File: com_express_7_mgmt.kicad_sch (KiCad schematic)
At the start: 64 parts, among them J1 Plug_Bus_CE7_EPT_401-51501-51, Q1 BSS138-7-F, Q2 BSS138-7-F, SW1 SW_1-1825027-1_THT, SW2 SW_1-1825027-1_THT, SW3 SW_DS04-254-1-01BK-SMT, U30 MAX16150A_SOT, U31 74AUP2G132, U32 TPS3840PL30DBVR, U33 74AUP2G132, U34 W25Q32FV_SOIC-8, U35 M24C64-F_DFN8

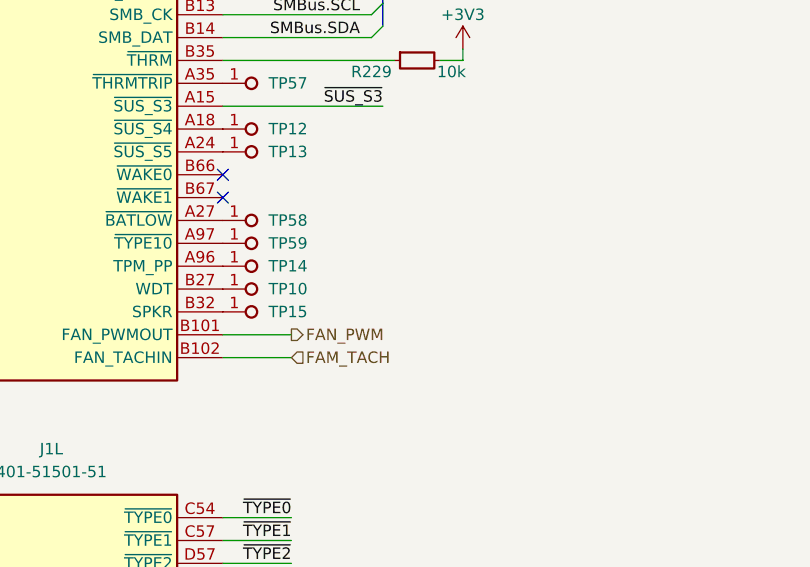
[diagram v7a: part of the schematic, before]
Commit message: [#57905] Add ADT7476AARQZ temperature/voltage/fan system monitor, LEDs
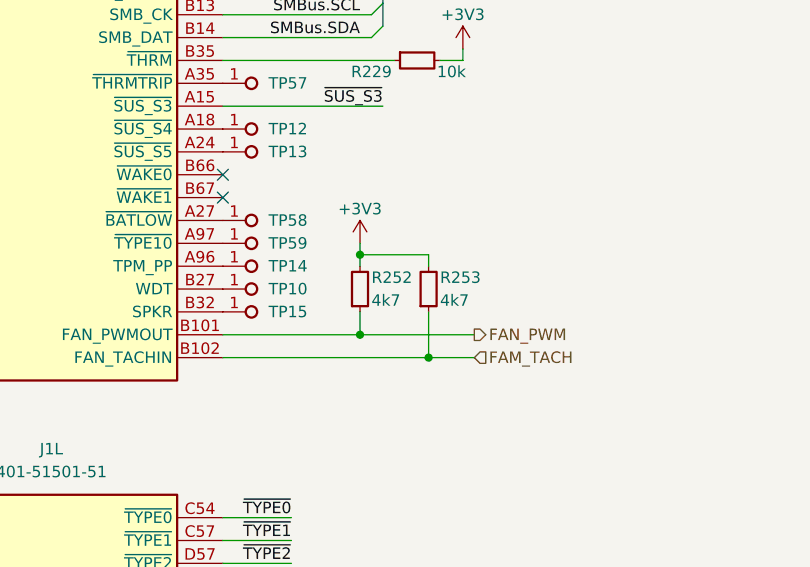
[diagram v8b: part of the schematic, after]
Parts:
- added R252, R253: R_4k7_0402, antmicro-footprints:R_0402_1005Metric, symbol antmicroResistors0402:R_4k7_0402
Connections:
- net +3V3: now also R252.2, R253.2
- net FAM_TACH: now also R253.1
- net FAN_PWM: now also R252.1
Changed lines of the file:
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@@
   (junction (at 217.17 78.74) (diameter 0) (color 0 0 0 0)
   )
+  (junction (at 91.44 184.15) (diameter 0) (color 0 0 0 0)
+  )
   (junction (at 356.87 193.04) (diameter 0) (color 0 0 0 0)
   )
@@
   (junction (at 336.55 41.91) (diameter 0) (color 0 0 0 0)
   )
+  (junction (at 91.44 193.04) (diameter 0) (color 0 0 0 0)
+  )
   (junction (at 228.6 218.44) (diameter 0) (color 0 0 0 0)
   )
@@
   )
   (junction (at 250.19 223.52) (diameter 0) (color 0 0 0 0)
+  )
+  (junction (at 99.06 195.58) (diameter 0) (color 0 0 0 0)
   )
   (junction (at 299.72 59.69) (diameter 0) (color 0 0 0 0)
@@
     (stroke (width 0) (type default))
   )
+  (wire (pts (xy 91.44 184.15) (xy 91.44 185.42))
+    (stroke (width 0) (type default))
+  )
   (wire (pts (xy 76.2 50.8) (xy 78.74 50.8))
     (stroke (width 0) (type default))
@@
     (stroke (width 0) (type default))
   )
+  (wire (pts (xy 91.44 182.88) (xy 91.44 184.15))
+    (stroke (width 0) (type default))
+  )
   (wire (pts (xy 311.15 190.5) (xy 323.85 190.5))
     (stroke (width 0) (type default))
@@
   )
   (wire (pts (xy 344.17 68.58) (xy 344.17 67.31))
+    (stroke (width 0) (type default))
+  )
+  (wire (pts (xy 99.06 184.15) (xy 99.06 185.42))
     (stroke (width 0) (type default))
   )
@@
     (stroke (width 0) (type default))
   )
+  (wire (pts (xy 91.44 184.15) (xy 99.06 184.15))
+    (stroke (width 0) (type default))
+  )
   (wire (pts (xy 280.67 137.16) (xy 283.21 137.16))
     (stroke (width 0) (type default))
@@
     (stroke (width 0) (type default))
   )
+  (wire (pts (xy 99.06 195.58) (xy 104.14 195.58))
+    (stroke (width 0) (type default))
+  )
   (bus (pts (xy 210.82 209.55) (xy 201.93 209.55))
     (stroke (width 0) (type default))
@@
     (stroke (width 0) (type default))
   )
+  (wire (pts (xy 91.44 190.5) (xy 91.44 193.04))
+    (stroke (width 0) (type default))
+  )
   (bus (pts (xy 316.23 207.01) (xy 316.23 204.47))
     (stroke (width 0) (type default))
@@
     (stroke (width 0) (type default))
   )
+  (wire (pts (xy 91.44 193.04) (xy 76.2 193.04))
+    (stroke (width 0) (type default))
+  )
   (wire (pts (xy 76.2 248.92) (xy 92.71 248.92))
     (stroke (width 0) (type default))
@@
     (stroke (width 0) (type default))
   )
-  (wire (pts (xy 83.82 193.04) (xy 76.2 193.04))
+  (wire (pts (xy 104.14 193.04) (xy 91.44 193.04))
     (stroke (width 0) (type default))
   )
@@
     (stroke (width 0) (type default))
   )
+  (wire (pts (xy 99.06 190.5) (xy 99.06 195.58))
+    (stroke (width 0) (type default))
+  )
   (wire (pts (xy 354.965 231.14) (xy 361.315 231.14))
     (stroke (width 0) (type default))
@@
     (stroke (width 0) (type default))
   )
-  (wire (pts (xy 76.2 195.58) (xy 83.82 195.58))
+  (wire (pts (xy 76.2 195.58) (xy 99.06 195.58))
     (stroke (width 0) (type default))
   )
@@
     (effects (font (size 1.27 1.27)) (justify right bottom))
   )
-  (hierarchical_label "FAM_TACH" (shape input) (at 83.82 195.58 0) (fields_autoplaced)
+  (hierarchical_label "FAM_TACH" (shape input) (at 104.14 195.58 0) (fields_autoplaced)
     (effects (font (size 1.27 1.27)) (justify left))
   )
@@
     (effects (font (size 1.27 1.27)) (justify left))
   )
-  (hierarchical_label "FAN_PWM" (shape output) (at 83.82 193.04 0) (fields_autoplaced)
+  (hierarchical_label "FAN_PWM" (shape output) (at 104.14 193.04 0) (fields_autoplaced)
     (effects (font (size 1.27 1.27)) (justify left))
   )
@@
     )
   )
+  (symbol (lib_id "antmicroResistors0402:R_4k7_0402") (at 91.44 190.5 90) (unit 1)
+    (in_bom yes) (on_board yes) (dnp no)
+    (property "Reference" "R252" (at 92.71 186.69 90)
+      (effects (font (size 1.27 1.27) (thickness 0.15)) (justify right))
+    )
+    (property "Value" "R_4k7_0402" (at 104.14 170.18 0)
+      (effects (font (size 1.27 1.27) (thickness 0.15)) (justify left bottom) hide)
+    )
+    (property "Footprint" "antmicro-footprints:R_0402_1005Metric" (at 106.68 170.18 0)
+      (effects (font (size 1.27 1.27) (thickness 0.15)) (justify left bottom) hide)
+    )
+    (property "Datasheet" "https://www.bourns.com/docs/product-datasheets/cr.pdf" (at 109.22 170.18 0)
+      (effects (font (size 1.27 1.27) (thickness 0.15)) (justify left bottom) hide)
+    )
+    (property "MPN" "CR0402-FX-4701GLF" (at 111.76 170.18 0)
+      (effects (font (size 1.27 1.27) (thickness 0.15)) (justify left bottom) hide)
+    )
+    (property "Manufacturer" "Bourns" (at 114.3 170.18 0)
+      (effects (font (size 1.27 1.27) (thickness 0.15)) (justify left bottom) hide)
+    )
+    (property "License" "Apache-2.0" (at 116.84 170.18 0)
+      (effects (font (size 1.27 1.27) (thickness 0.15)) (justify left bottom) hide)
+    )
+    (property "Author" "Antmicro" (at 119.38 170.18 0)
+      (effects (font (size 1.27 1.27) (thickness 0.15)) (justify left bottom) hide)
+    )
+    (property "Val" "4k7" (at 92.71 189.23 90)
+      (effects (font (size 1.27 1.27) (thickness 0.15)) (justify right))
+    )
+    (property "Tolerance" "1%" (at 101.6 170.18 0)
+      (effects (font (size 1.27 1.27)) (justify left bottom) hide)
+    )
+    (pin "2")
+    (pin "1")
+    (instances
+      (project "com-express-7-baseboard"
+        (path "/1b8c34da-dad5-4b0b-8c4b-45db766c4dfa/ec04a123-aeba-4efb-8d03-9c06245c1fcc"
+          (reference "R252") (unit 1)
+        )
+      )
+    )
+  )
   (symbol (lib_id "antmicropower:GND") (at 269.24 45.72 0) (unit 1)
     (in_bom yes) (on_board yes) (dnp no)
@@
         (path "/1b8c34da-dad5-4b0b-8c4b-45db766c4dfa/ec04a123-aeba-4efb-8d03-9c06245c1fcc"
           (reference "TP56") (unit 1)
+        )
+      )
+    )
+  )
+  (symbol (lib_id "antmicropower:+3V3") (at 91.44 182.88 0) (unit 1)
+    (in_bom yes) (on_board yes) (dnp no)
+    (property "Reference" "#PWR0306" (at 106.68 182.88 0)
+      (effects (font (size 1.27 1.27) (thickness 0.15)) (justify left bottom) hide)
+    )
+    (property "Value" "+3V3" (at 91.44 179.07 0)
+      (effects (font (size 1.27 1.27) (thickness 0.15)))
+    )
+    (property "Footprint" "" (at 106.68 190.5 0)
+      (effects (font (size 1.27 1.27) (thickness 0.15)) (justify left bottom) hide)
+    )
+    (property "Datasheet" "" (at 106.68 193.04 0)
+      (effects (font (size 1.27 1.27) (thickness 0.15)) (justify left bottom) hide)
+    )
+    (property "Author" "Antmicro" (at 106.68 185.42 0)
+      (effects (font (size 1.27 1.27) (thickness 0.15)) (justify left bottom) hide)
+    )
+    (property "License" "Apache-2.0" (at 106.68 187.96 0)
+      (effects (font (size 1.27 1.27) (thickness 0.15)) (justify left bottom) hide)
+    )
+    (pin "1")
+    (instances
+      (project "com-express-7-baseboard"
+        (path "/1b8c34da-dad5-4b0b-8c4b-45db766c4dfa/ec04a123-aeba-4efb-8d03-9c06245c1fcc"
+          (reference "#PWR0306") (unit 1)
         )
       )
@@
         )
       )
+    )
+  )
+  (symbol (lib_id "antmicroResistors0402:R_4k7_0402") (at 99.06 190.5 90) (unit 1)
+    (in_bom yes) (on_board yes) (dnp no)
+    (property "Reference" "R253" (at 100.33 186.69 90)
+      (effects (font (size 1.27 1.27) (thickness 0.15)) (justify right))
+    )
+    (property "Value" "R_4k7_0402" (at 111.76 170.18 0)
+      (effects (font (size 1.27 1.27) (thickness 0.15)) (justify left bottom) hide)
+    )
+    (property "Footprint" "antmicro-footprints:R_0402_1005Metric" (at 114.3 170.18 0)
+      (effects (font (size 1.27 1.27) (thickness 0.15)) (justify left bottom) hide)
+    )
+    (property "Datasheet" "https://www.bourns.com/docs/product-datasheets/cr.pdf" (at 116.84 170.18 0)
+      (effects (font (size 1.27 1.27) (thickness 0.15)) (justify left bottom) hide)
+    )
+    (property "MPN" "CR0402-FX-4701GLF" (at 119.38 170.18 0)
+      (effects (font (size 1.27 1.27) (thickness 0.15)) (justify left bottom) hide)
+    )
+    (property "Manufacturer" "Bourns" (at 121.92 170.18 0)
+      (effects (font (size 1.27 1.27) (thickness 0.15)) (justify left bottom) hide)
+    )
+    (property "License" "Apache-2.0" (at 124.46 170.18 0)
+      (effects (font (size 1.27 1.27) (thickness 0.15)) (justify left bottom) hide)
+    )
+    (property "Author" "Antmicro" (at 127 170.18 0)
+      (effects (font (size 1.27 1.27) (thickness 0.15)) (justify left bottom) hide)
+    )
+    (property "Val" "4k7" (at 100.33 189.23 90)
+      (effects (font (size 1.27 1.27) (thickness 0.15)) (justify right))
+    )
+    (property "Tolerance" "1%" (at 109.22 170.18 0)
+      (effects (font (size 1.27 1.27)) (justify left bottom) hide)
+    )
+    (pin "2")
+    (pin "1")
+    (instances
+      (project "com-express-7-baseboard"
+        (path "/1b8c34da-dad5-4b0b-8c4b-45db766c4dfa/ec04a123-aeba-4efb-8d03-9c06245c1fcc"
+          (reference "R253") (unit 1)
+        )
+      )
